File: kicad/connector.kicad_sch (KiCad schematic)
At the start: 1 part, among them J1 500 card edge

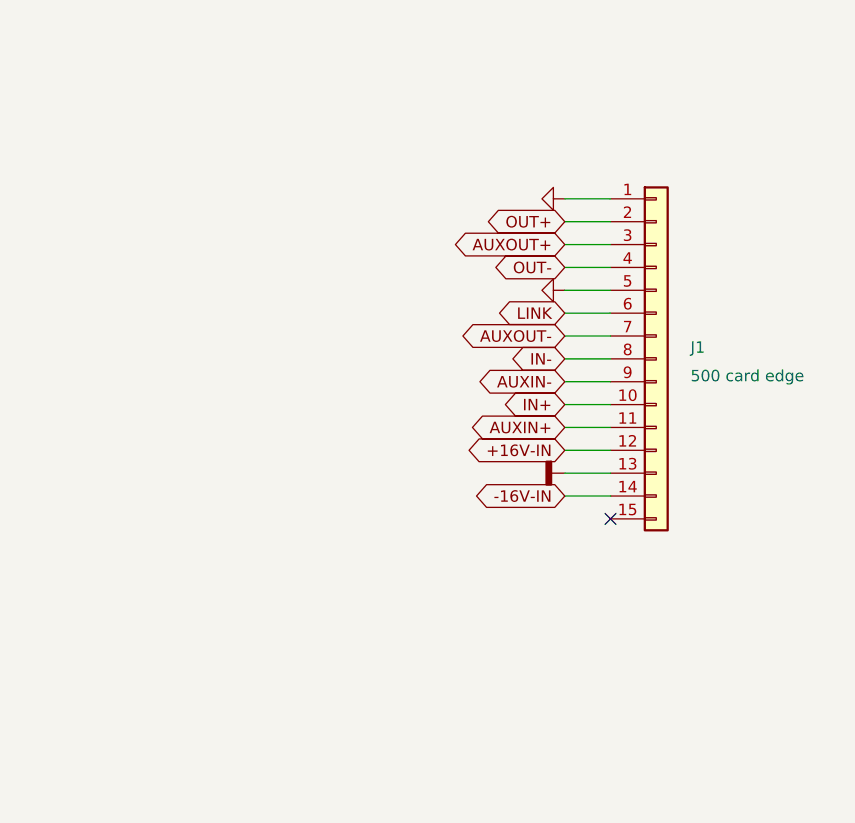
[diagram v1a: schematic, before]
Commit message: Add reorganised schematic to split files.
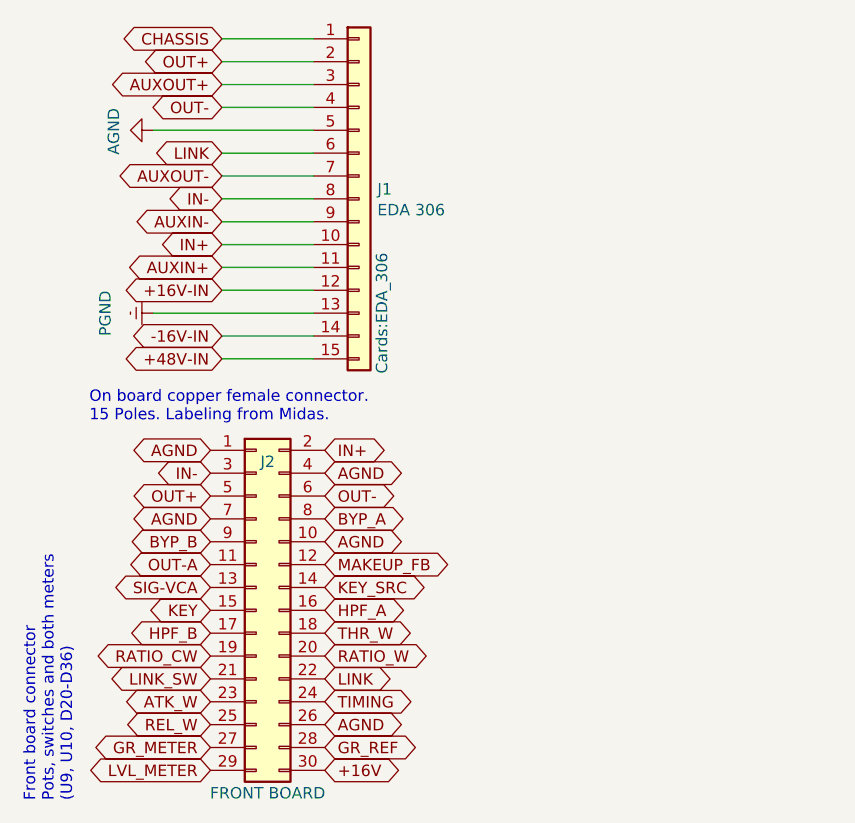
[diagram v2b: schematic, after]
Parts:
- added J2: FRONT BOARD, Connector_IDC:IDC-Header_2x15_P2.54mm_Vertical, symbol Connector_Generic:Conn_02x15_Odd_Even
- J1: value 500 card edge -> EDA 306; footprint (none) -> Cards:EDA_306
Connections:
- net AGND: now also J2.1 (Pin_1), J2.10 (Pin_10), J2.26 (Pin_26), J2.4 (Pin_4), J2.7 (Pin_7)
- net IN+: now also J2.2 (Pin_2)
- net IN-: now also J2.3 (Pin_3)
- net LINK: now also J2.22 (Pin_22)
- net OUT+: now also J2.5 (Pin_5)
- net OUT-: now also J2.6 (Pin_6)
- net +48V-IN: now reaches J1.15 (Pin_15)
- new net +16V: J2.30 (Pin_30)
- new net ATK_W: J2.23 (Pin_23)
- new net BYP_A: J2.8 (Pin_8)
- new net BYP_B: J2.9 (Pin_9)
- new net GR_METER: J2.27 (Pin_27)
- new net GR_REF: J2.28 (Pin_28)
- new net HPF_A: J2.16 (Pin_16)
- new net HPF_B: J2.17 (Pin_17)
- new net KEY: J2.15 (Pin_15)
- new net KEY_SRC: J2.14 (Pin_14)
- new net LINK_SW: J2.21 (Pin_21)
- new net LVL_METER: J2.29 (Pin_29)
- new net MAKEUP_FB: J2.12 (Pin_12)
- new net OUT-A: J2.11 (Pin_11)
- new net RATIO_CW: J2.19 (Pin_19)
- new net RATIO_W: J2.20 (Pin_20)
- new net REL_W: J2.25 (Pin_25)
- new net SIG-VCA: J2.13 (Pin_13)
- new net THR_W: J2.18 (Pin_18)
- new net TIMING: J2.24 (Pin_24)
- no-connect marks 1 -> 0
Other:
- note added: "Front board connector Pots, switches and both meters (U9, U10, D20-D36)"
- note added: "On board copper female connector. 15 Poles. Labeling from Midas."
